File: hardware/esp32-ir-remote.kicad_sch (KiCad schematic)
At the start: 72 parts, among them J2 USB_C_Receptacle_USB2.0_14P, J3 Qwiic_I2C, J4 GPIO_PWR, J5 EXT_IR, J6 JTAG, Q1 2N7002, Q2 2N7002, Q3 IRLML6344, Q4 2N7002, Q5 2N7002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

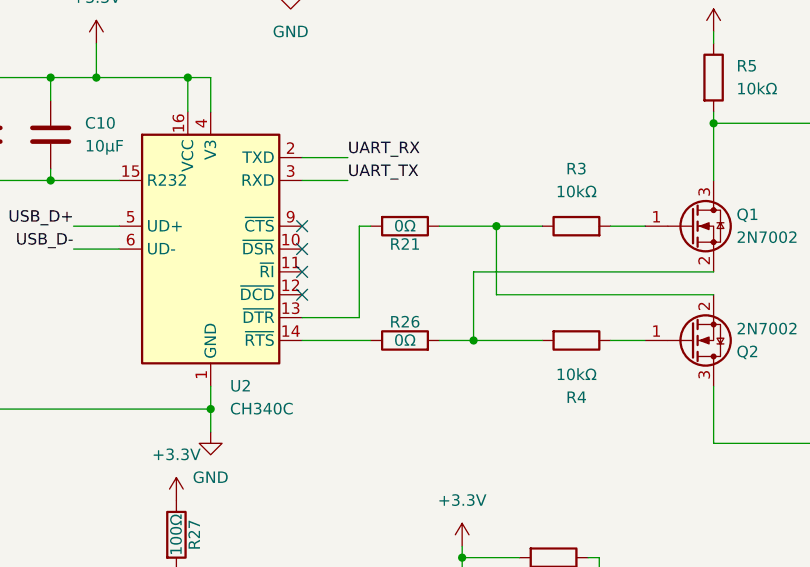
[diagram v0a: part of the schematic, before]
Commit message: Auto-reset bypass links R21/R26: 0R -> 470R; purge unused lib symbols
Nick OK'd larger changes in favor of circuit correctness. The FET swap's
one real regression: holding RESET/BOOT with the port idle forward-biases
the 2N7002 body diode (RTS->EN / DTR->GPIO0) and, through 0R links,
shorted a CH340C pin to GND at ~25mA (the BJT circuit leaked 0.27mA via
its 10k base path). Making the bypass links 470R (C23179, 0603, Basic,
2.3M stock) caps that at ~5mA while staying transparent to auto-reset:
EN/GPIO0 lows ~0.15V vs 0.825V VIL (5x margin even at worst-case Rds),
EN-cap discharge 470R x 1uF = 0.5ms inside esptool's ~100ms pulses, and
desolder-to-disable is preserved. BOM line count unchanged (0R line
becomes a 470R 0603 line).

R3/R4 gate resistors deliberately kept: FET gates draw no DC current so
they are electrically invisible, they add gate-ESD robustness, and
removing them would be copper churn on a routed board for zero gain.

Hygiene: removed 5 unused embedded lib symbols from the schematic (4
orphaned PCM_JLCPCB leftovers from the H1.2 conversion - one carrying
cross-contaminated 0R-resistor/2N7002 metadata - plus the now-unused
Q_NPN_BEC). Netlist verified unaffected. The locally-derived R_1 symbol
(referenced via lib_name) is kept.

Silk label updated to "R21/R26: auto-rst 470R"; gerbers + zip + renders
regenerated with kicad-cli 9.0.6. Copper layers verified geometrically
identical to the previous package (diff is net-name attributes from the
PR #4 renames plus timestamps); silkscreen layers no longer carry the
pads-on-silk plot noise from the original pcbnew export.

Verification (kicad/kicad:9.0.6; reads clean under 10.0.2): ERC 9 = 2
pre-existing J4 GPIO25/26 errors + 7 dual-label warnings; netlist diff
is R21/R26 value/LCSC only; DRC 3 accepted errors / 7 pour notices /
schematic parity 0; netlist<->PCB partition check identical.

https://claude.ai/code/session_01NnkrUCiFVFngztSgzPXbfT
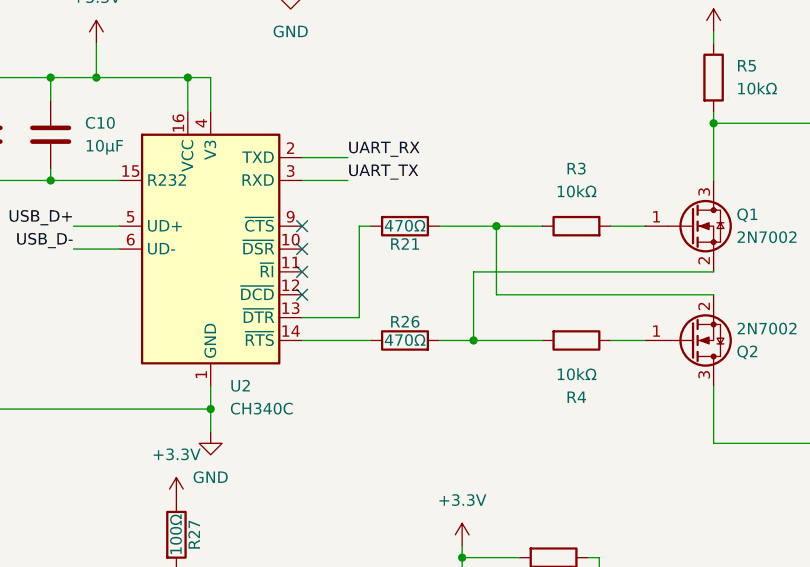
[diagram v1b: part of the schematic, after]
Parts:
- R21, R26: value 0Ω -> 470Ω; LCSC C21189 -> C23179
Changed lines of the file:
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@@
 			(effects (font (size 1.27 1.27)))
 		)
-		(property "Value" "0Ω"
+		(property "Value" "470Ω"
 			(at 144.78 132.08 90.0)
 			(effects (font (size 1.27 1.27)))
@@
 			(effects (font (size 1.27 1.27)) (hide yes))
 		)
-		(property "Datasheet" "https://www.lcsc.com/datasheet/lcsc_datasheet_2411221126_UNI-ROYAL-Uniroyal-Elec-0603WAF0000T5E_C21189.pdf"
+		(property "Datasheet" "https://www.lcsc.com/datasheet/lcsc_datasheet_2206010116_UNI-ROYAL-Uniroyal-Elec-0603WAF4700T5E_C23179.pdf"
 			(at 144.78 132.08 0)
 			(effects (font (size 1.27 1.27)) (hide yes))
 		)
-    (property "LCSC" "C21189" (at 144.78 132.08 0)
+    (property "LCSC" "C23179" (at 144.78 132.08 0)
       (effects (font (size 1.27 1.27)) (hide yes))
     )
@@
 			(effects (font (size 1.27 1.27)))
 		)
-		(property "Value" "0Ω"
+		(property "Value" "470Ω"
 			(at 144.78 144.78 90.0)
 			(effects (font (size 1.27 1.27)))
@@
 			(effects (font (size 1.27 1.27)) (hide yes))
 		)
-		(property "Datasheet" "https://www.lcsc.com/datasheet/lcsc_datasheet_2411221126_UNI-ROYAL-Uniroyal-Elec-0603WAF0000T5E_C21189.pdf"
+		(property "Datasheet" "https://www.lcsc.com/datasheet/lcsc_datasheet_2206010116_UNI-ROYAL-Uniroyal-Elec-0603WAF4700T5E_C23179.pdf"
 			(at 144.78 144.78 0)
 			(effects (font (size 1.27 1.27)) (hide yes))
 		)
-    (property "LCSC" "C21189" (at 144.78 144.78 0)
+    (property "LCSC" "C23179" (at 144.78 144.78 0)
       (effects (font (size 1.27 1.27)) (hide yes))
     )

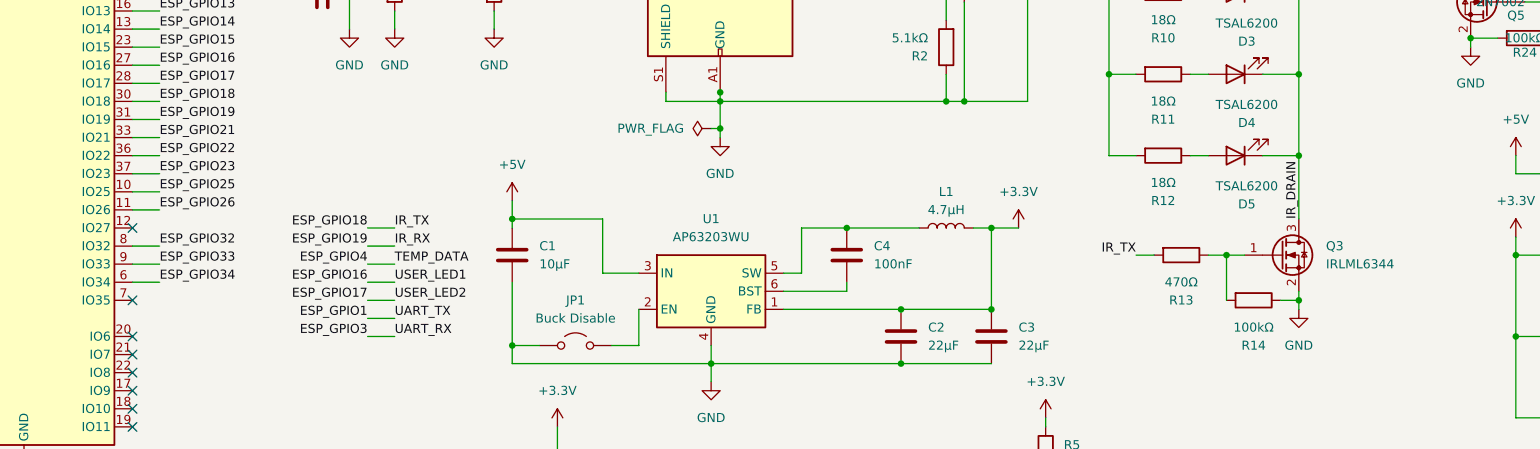
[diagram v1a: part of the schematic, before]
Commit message: Schematic: Q3 -> AO3400A, SW1/SW2 -> TS-1187A (both Basic); ERC 0/7
Cost/availability pass before the fab order (Nick OK'd part swaps):
- Q3 IR driver: IRLML6344 (C53550, Extended) -> AO3400A (C20917, Basic,
  1.7M stock). Same SOT-23 pinout, logic-level, 48mOhm@2.5V vs 29mOhm
  - 8mV extra drop at the 0.42A IR burst, immaterial. Field-only change.
- SW1/SW2: TS-1088R (C455280, Extended) -> XKB TS-1187A-B-A-B (C318884,
  Basic, 1.8M stock, $0.02). New footprint lib:SW-SMD_TS-1187A-5.1x5.1
  drawn from the datasheet land pattern (pads 1.0x0.75 at +/-3.0/+/-1.875).
  Datasheet circuit: same-row terminals are internally common, so the two
  rows are numbered 1/1 and 2/2 - the generic 2-pin SW_Push symbol maps
  unchanged. PCB swap follows in the next commit.
- IO25/IO26 hygiene: the two 'J4' ERC errors were orphan label+wire stubs
  left when GPIO25/26 were dropped from J4 (the roadmap's claimed
  no_connects were never actually placed). Stubs removed, real no_connect
  markers added: ERC is now 0 errors / 7 deliberate dual-label warnings.

Netlist regenerated (KiCad 9.0.7 container): diff is electrically empty -
net renumbering, IO25/26 single-pin nets renamed unconnected-(U3-IO25/26),
plus the intended Q3/SW1/SW2 field changes.

https://claude.ai/code/session_01Koc1vNGxodNG5CwHMUeuXW
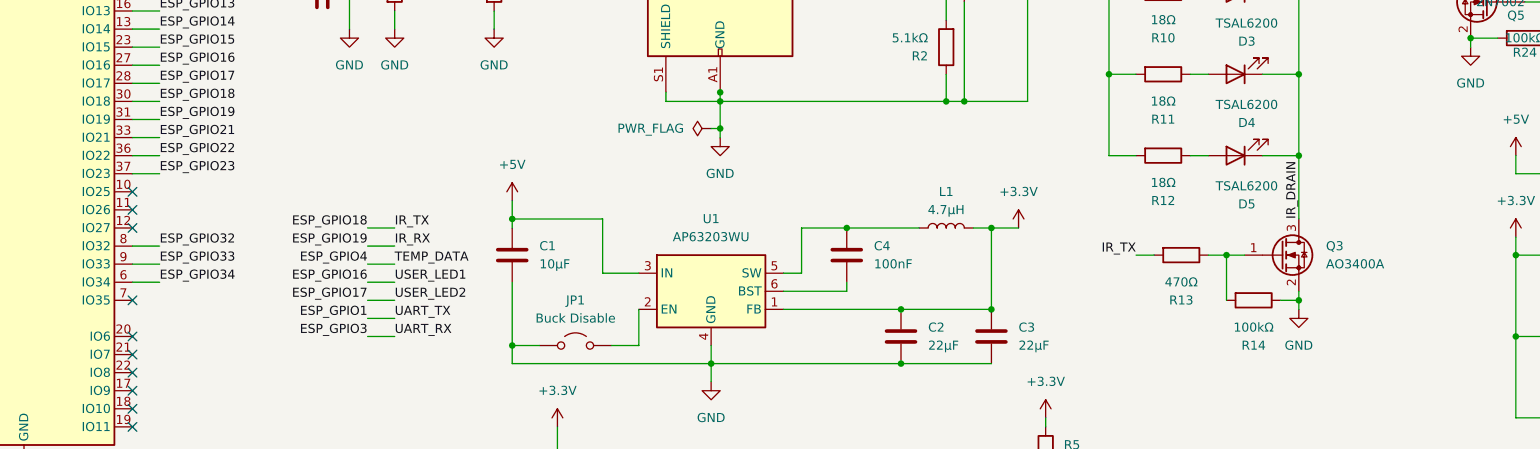
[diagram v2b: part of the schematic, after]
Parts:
- Q3: value IRLML6344 -> AO3400A; LCSC C53550 -> C20917
- SW1, SW2: footprint JLC-MCP:SW-SMD_L3.9-W3.0-P4.45 -> lib:SW-SMD_TS-1187A-5.1x5.1; LCSC C455280 -> C318884
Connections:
- net ESP_GPIO25: no longer names the net of U3.10 (IO25)
- net ESP_GPIO26: no longer names the net of U3.11 (IO26)
- no-connect marks 18 -> 20
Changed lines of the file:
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@@
 	)
 	(no_connect
+		(at 50.8 78.74)
+	)
+	(no_connect
+		(at 50.8 81.28)
+	)
+	(no_connect
 		(at 133.35 134.62)
 	)
@@
 			(effects (font (size 1.27 1.27)) (justify left))
 		)
-		(property "Value" "IRLML6344"
+		(property "Value" "AO3400A"
 			(at 218.44 88.8999 0)
 			(effects (font (size 1.27 1.27)) (justify left))
@@
 			(effects (font (size 1.27 1.27)) (hide yes))
 		)
-		(property "LCSC" "C53550"
+		(property "LCSC" "C20917"
 			(at 212.09 87.63 0)
 			(effects (font (size 1.27 1.27)) (hide yes))
@@
 			(effects (font (size 1.27 1.27)))
 		)
-		(property "Footprint" "JLC-MCP:SW-SMD_L3.9-W3.0-P4.45"
+		(property "Footprint" "lib:SW-SMD_TS-1187A-5.1x5.1"
 			(at 259.08 148.59 0)
 			(effects (font (size 1.27 1.27)) (hide yes))
@@
 			(effects (font (size 1.27 1.27)) (hide yes))
 		)
-		(property "LCSC" "C455280"
+		(property "LCSC" "C318884"
 			(at 259.08 153.67 0)
 			(effects (font (size 1.27 1.27)) (hide yes))
@@
 			(effects (font (size 1.27 1.27)))
 		)
-		(property "Footprint" "JLC-MCP:SW-SMD_L3.9-W3.0-P4.45"
+		(property "Footprint" "lib:SW-SMD_TS-1187A-5.1x5.1"
 			(at 259.08 137.16 0)
 			(effects (font (size 1.27 1.27)) (hide yes))
@@
 			(effects (font (size 1.27 1.27)) (hide yes))
 		)
-		(property "LCSC" "C455280"
+		(property "LCSC" "C318884"
 			(at 259.08 142.24 0)
 			(effects (font (size 1.27 1.27)) (hide yes))
@@
 	)
 	(wire
-		(pts (xy 50.8 78.74) (xy 54.61 78.74))
-		(stroke (width 0) (type default))
-	)
-	(wire
-		(pts (xy 50.8 81.28) (xy 54.61 81.28))
-		(stroke (width 0) (type default))
-	)
-	(wire
 		(pts (xy 50.8 86.36) (xy 54.61 86.36))
 		(stroke (width 0) (type default))
@@
 		(effects (font (size 1.27 1.27)) (justify left bottom))
 	)
-	(label "ESP_GPIO25"
-		(at 54.61 78.74 0)
-		(effects (font (size 1.27 1.27)) (justify left bottom))
-	)
-	(label "ESP_GPIO26"
-		(at 54.61 81.28 0)
-		(effects (font (size 1.27 1.27)) (justify left bottom))
-	)

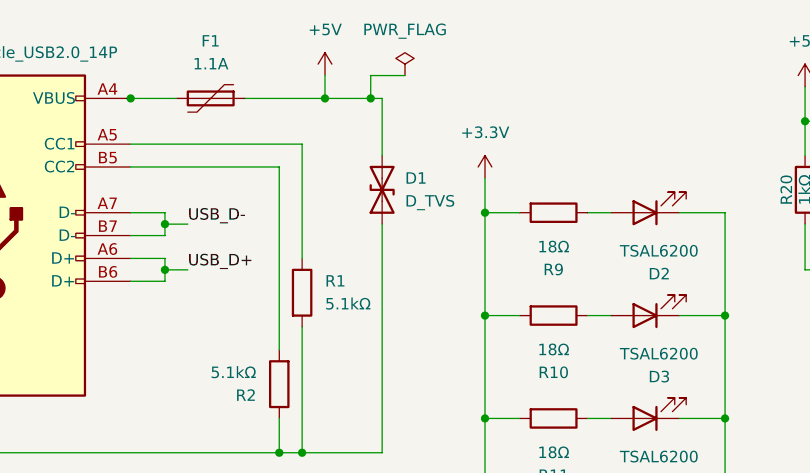
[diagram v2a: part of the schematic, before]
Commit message: Polarity automation + fix inverted D1 TVS marking (found by it)
Nick: 'I don't want you to rely on me for correctness' — so:

1. Polarity truth table (gating CI check): 66 pin->net invariants across
   all 23 polarized/orientation-critical parts, locked from the reviewed
   v1.4 design. Any flipped diode / swapped FET pinout / rewired power
   pin fails CI naming the exact pin.

2. CPL rotation corrections in fab-outputs.py: JLC per-package
   zero-orientation offsets applied (SOT-23 +270, TSOT-23 +180, SOIC
   +270, ESP32-WROOM +270; JLCKicadTools DB). Every assembled footprint
   must be classified (offset or symmetric regex) or CPL generation
   refuses. New orientation-report.csv = mechanical JLC-preview
   checklist, published with the fab package.

3. BUG FOUND BY THIS WORK - D1 TVS polarity marking was inverted: the
   D_SMB footprint prints its cathode band at pad 1 which was wired to
   GND; a unidirectional SMBJ5.0A clamp needs cathode on +5V. The
   bidirectional D_TVS symbol hid this from every electrical check, and
   the old kit note ('band toward F1') was geometrically ambiguous
   (F1 is east, pads run north-south). Hand-soldering to the board's own
   marking = TVS forward across the rail = board won't power.
   Fix: D1 rotated 180 in place (sch 90->270, PCB 90->270 + pad nets
   swapped, netlist nodes swapped) - pads are symmetric so copper is
   untouched (pad positions verified identical); the silk band now marks
   the +5V pad. Kit + bring-up instructions updated. Polarity table
   locks D1.1(K)=+5V.

https://claude.ai/code/session_015CjxBQcs2mXfovZaBKMbKU
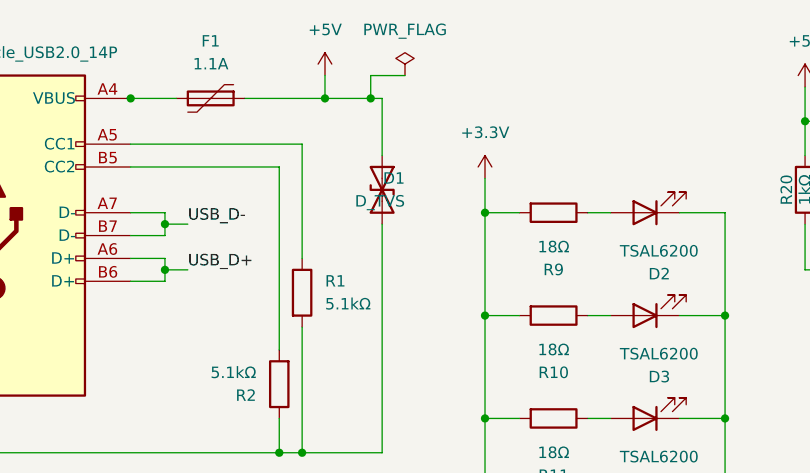
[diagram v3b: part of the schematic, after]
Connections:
- net +5V: now also D1.1 (A1); no longer D1.2 (A2)
- net GND: now also D1.2 (A2); no longer D1.1 (A1)
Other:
- moved on the sheet: D1
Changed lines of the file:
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@@
 	(symbol
 		(lib_id "Device:D_TVS")
-		(at 176.53 36.83 90)
+		(at 176.53 36.83 270)
 		(unit 1)
 		(exclude_from_sim no)

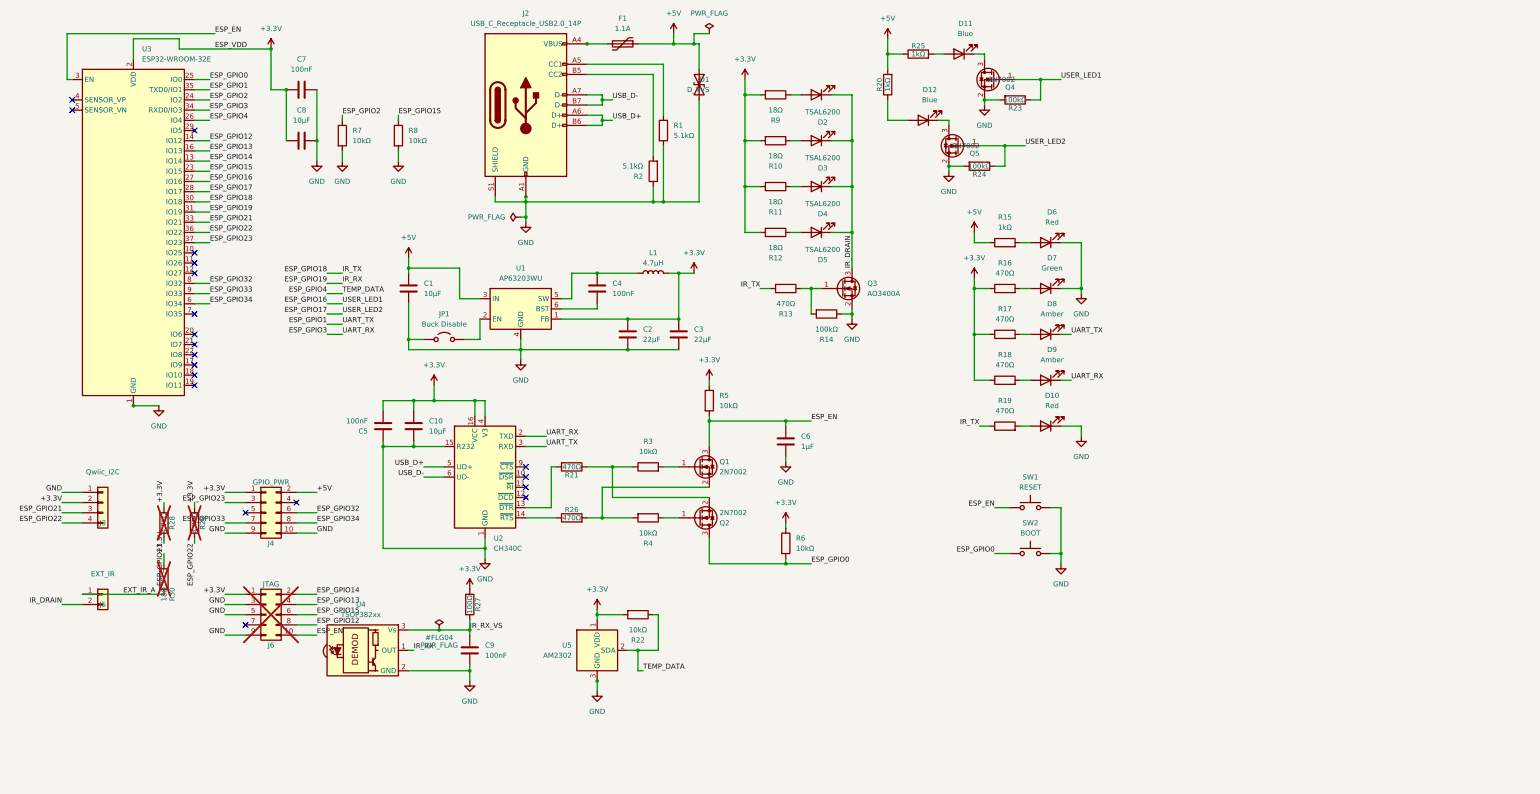
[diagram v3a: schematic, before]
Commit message: wip(sch): board v2 schematic surgery — 20 deletes + golden netlist verifier
Autonomous build toward the C3 redesign. Deleted the 20 removed parts
(CH340 + auto-reset, TX/RX LEDs, JTAG, Qwiic, buck inductor + bootstrap cap,
DHT pullup, user-LED FET drivers) — 52 components remain, file exports a
valid netlist. Added scripts/ci/golden_netlist_v2.py: the explicit pin-set
spec of every intended v2 net + a name-agnostic checker. 16/36 nets already
match; 20 remain (the U1/U3/U5 swaps + rewire). WIP — not pushed; CI stays
green on the last pushed commit until the schematic+PCB land together.
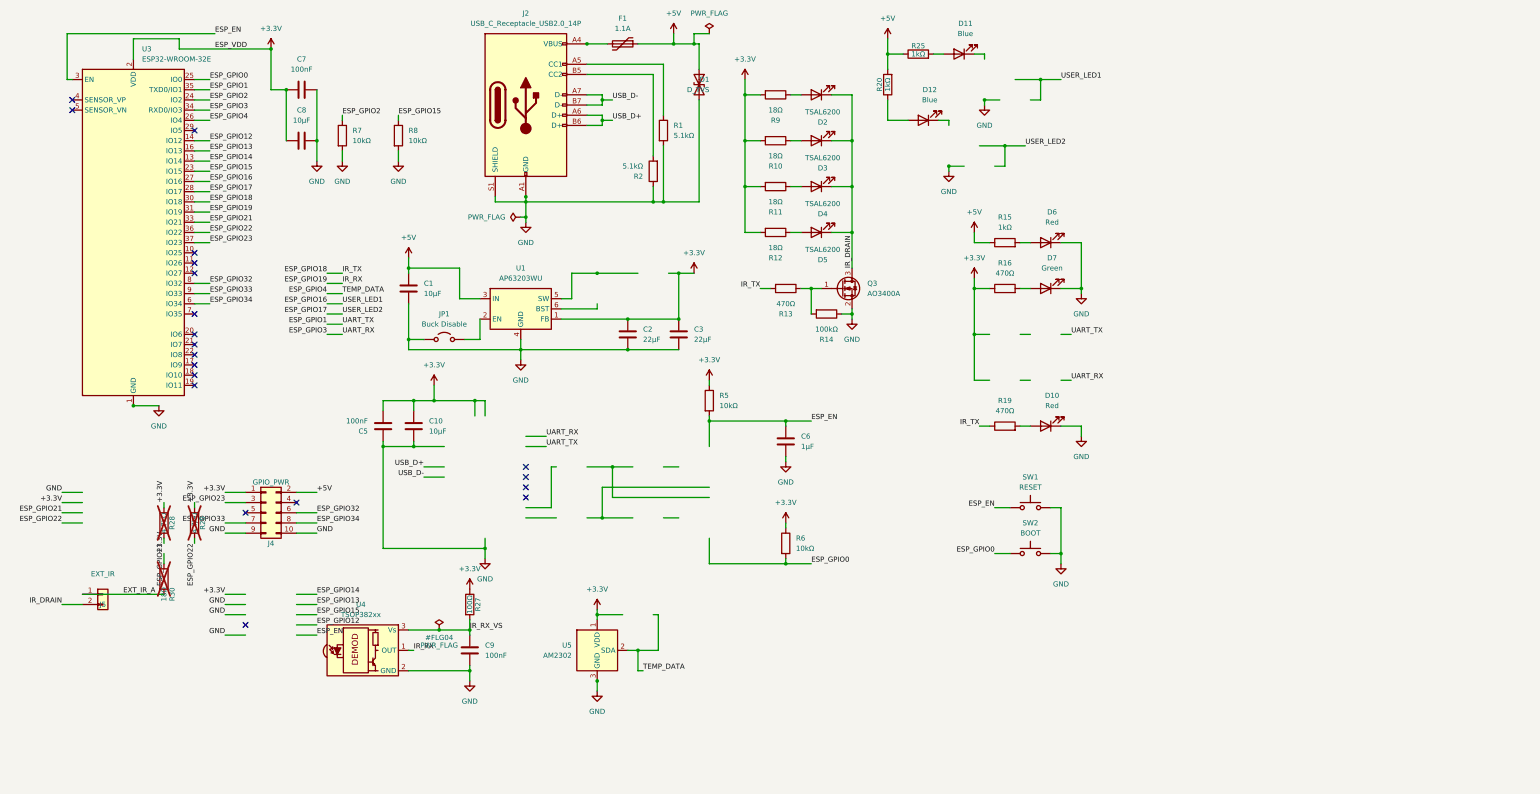
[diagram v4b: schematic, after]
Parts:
- removed C4: 100nF, Capacitor_SMD:C_0603_1608Metric, symbol Device:C
- removed D8, D9: Amber, LED_THT:LED_D3.0mm, symbol Device:LED
- removed J3: Qwiic_I2C, Connector_JST:JST_SH_SM04B-SRSS-TB_1x04-1MP_P1.00mm_Horizontal, symbol Connector_Generic:Conn_01x04
- removed J6: JTAG, Connector_PinHeader_2.54mm:PinHeader_2x05_P2.54mm_Vertical, symbol Connector_Generic:Conn_02x05_Odd_Even
- removed L1: 4.7µH, lib:IND-SMD_L6.7-W6.7, symbol Device:L
- removed Q1, Q2, Q4, Q5: 2N7002, Package_TO_SOT_SMD:SOT-23, symbol Transistor_FET:Q_NMOS_GSD
- removed R17, R18: 470Ω, Resistor_SMD:R_0805_2012Metric, symbol Device:R
- removed R21, R26: 470Ω, Resistor_SMD:R_0603_1608Metric, symbol Device:R
- removed R22: 10kΩ, Resistor_SMD:R_1206_3216Metric, symbol Device:R
- removed R23, R24: 100kΩ, Resistor_SMD:R_0603_1608Metric, symbol Device:R
- removed R3, R4: 10kΩ, Resistor_SMD:R_1206_3216Metric, symbol Device:R
- removed U2: CH340C, Package_SO:SOIC-16_3.9x9.9mm_P1.27mm, symbol Interface_USB:CH340C
